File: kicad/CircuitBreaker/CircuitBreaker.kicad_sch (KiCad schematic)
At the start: 57 parts, among them J1 PH2.54, J10 Conn_01x04_uplink, J4 PH2.54, J5 Conn_01x04_downlink, J6 Conn_01x04_downlink, J7 PH2.54, J9 Conn_01x04_uplink, SW1 usbIAP, T1 CT104D, T2 CT104D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

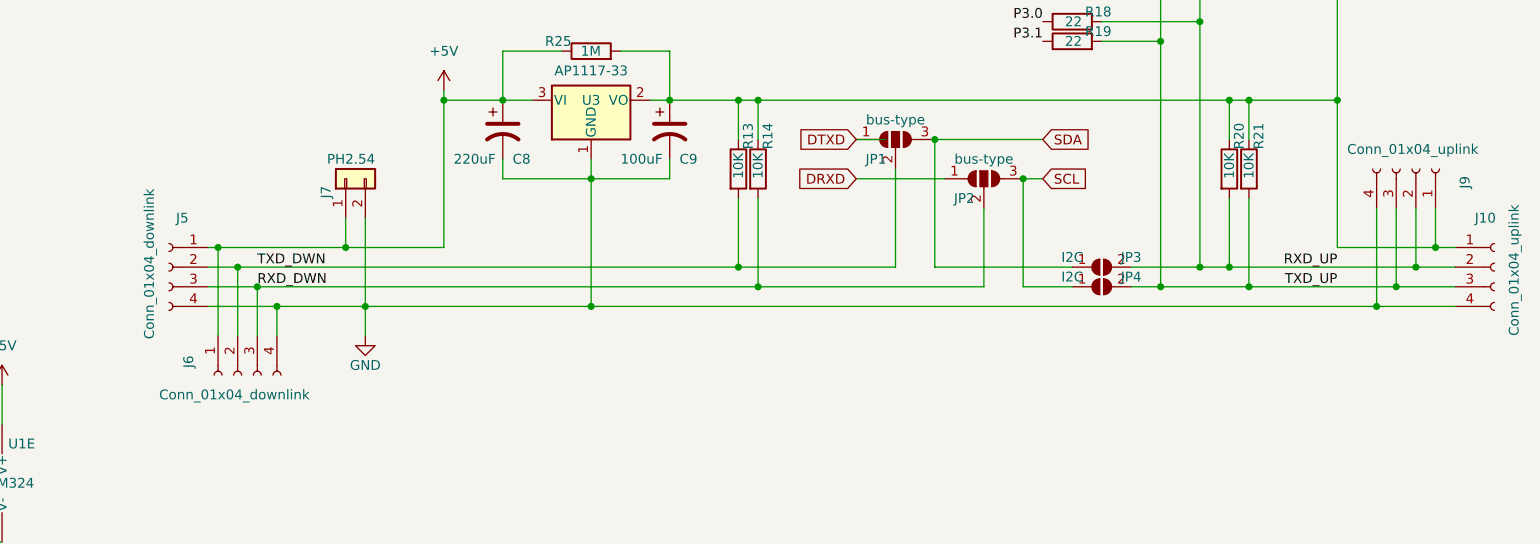
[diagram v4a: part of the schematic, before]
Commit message: net mapped to pcb
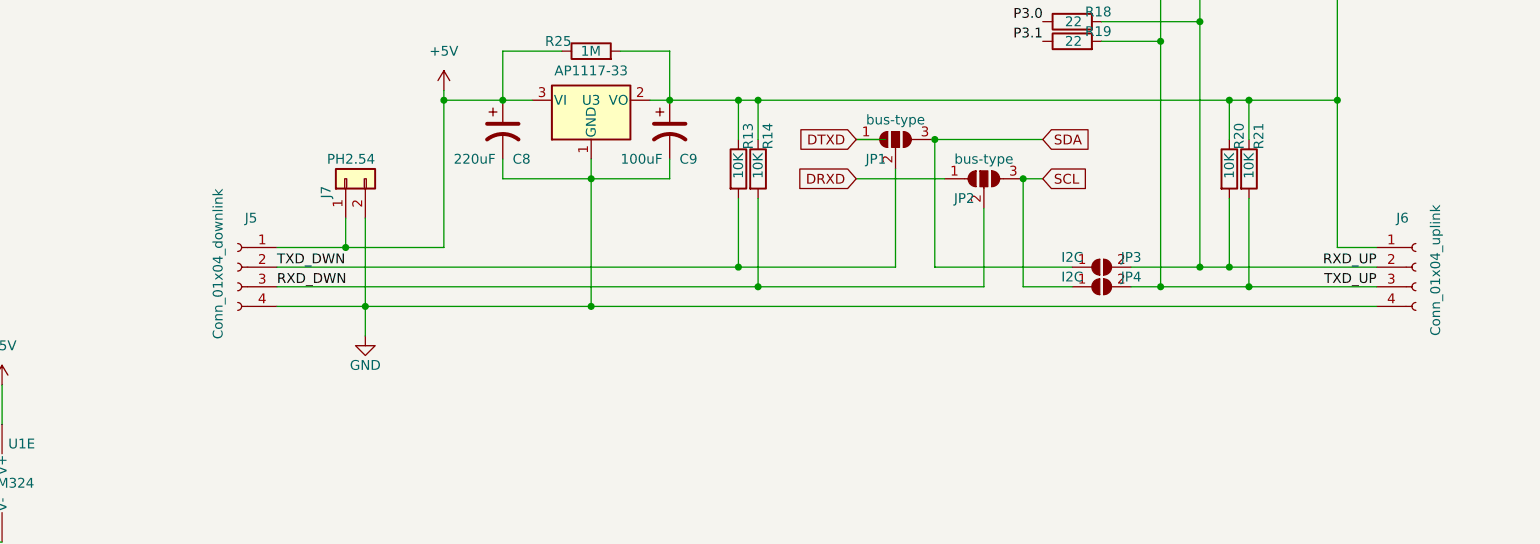
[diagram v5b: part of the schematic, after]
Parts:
- removed J6: Conn_01x04_downlink, Connector_PinHeader_2.00mm:PinHeader_1x04_P2.00mm_Vertical, symbol Connector:Conn_01x04_Female
- removed J9: Conn_01x04_uplink, Connector_PinSocket_2.00mm:PinSocket_1x04_P2.00mm_Vertical, symbol Connector:Conn_01x04_Female
- C1, C10, C2, C3, C4, C5, C6: footprint Capacitor_SMD:C_0201_0603Metric -> Capacitor_SMD:C_0603_1608Metric
- J7: footprint Connector_PinSocket_2.54mm:PinSocket_1x02_P2.54mm_Vertical_SMD_Pin1Left -> Connector_PinHeader_2.54mm:PinHeader_1x02_P2.54mm_Vertical
- R10, R11, R12, R13, R14, R15, R17, R18, R19, R20, R21, R22, R23, R24, R9: footprint Resistor_SMD:R_0201_0603Metric -> Resistor_SMD:R_0603_1608Metric
- R16: footprint Resistor_SMD:R_0201_0603Metric -> Resistor_SMD:R_0805_2012Metric
- renumbered J10 to J6
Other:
- moved on the sheet: J5, J6

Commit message: pcb rev
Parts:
- added D1: green, LED_SMD:LED_0603_1608Metric, symbol Device:LED
- added D2: blue, LED_SMD:LED_0603_1608Metric, symbol Device:LED
- added R26, R27: 4K7, Resistor_SMD:R_0603_1608Metric, symbol Device:R
- JP5, JP6: footprint Jumper:SolderJumper-2_P1.3mm_Open_RoundedPad1.0x1.5mm -> Jumper:SolderJumper-2_P1.3mm_Bridged_RoundedPad1.0x1.5mm
- R1, R2, R3, R7: footprint Resistor_THT:R_Axial_DIN0204_L3.6mm_D1.6mm_P1.90mm_Vertical -> Resistor_THT:R_Axial_DIN0204_L3.6mm_D1.6mm_P7.62mm_Horizontal
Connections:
- net +5V: now also D1.2 (A), D2.2 (A)
- net at U2.17 (P3.6/ADC14/RxD_2): now also R27.1
- net at U2.18 (P3.7/INT3/TxD_2): now also R26.1
- new net: D2.1 (K), R27.2
- new net: D1.1 (K), R26.2
- no-connect marks 27 -> 25
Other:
- moved on the sheet: C1, C10, C2, C3, C4, C5, C6, C7, C8, C9, J1, J4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

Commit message: pcb all connected
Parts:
- R25: value 1M -> 5vUP
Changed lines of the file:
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@@
       (effects (font (size 1.27 1.27)) (justify left))
     )
-    (property "Value" "1M" (id 1) (at 151.13 119.38 90)
+    (property "Value" "5vUP" (id 1) (at 151.13 119.38 90)
       (effects (font (size 1.27 1.27)) (justify left))
     )
@@
     )
     (path "/b9254481-42de-41b8-8b47-4a505cebb15c"
-      (reference "R25") (unit 1) (value "1M") (footprint "Resistor_SMD:R_0805_2012Metric")
+      (reference "R25") (unit 1) (value "5vUP") (footprint "Resistor_SMD:R_0805_2012Metric")
     )
     (path "/e07fefd4-5202-4e30-b6e7-2e0271b2c212"

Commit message: silklayers review
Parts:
- D1: value green -> grn
- D2: value blue -> blu
- J5: value Conn_01x04_downlink -> downlink
- J6: value Conn_01x04_uplink -> uplink
- J7: value PH2.54 -> PWN-In-5v
- U2: value STC8H8K64U-45I-TSSOP20 -> STC8H8K64U
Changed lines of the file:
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@@
       (effects (font (size 1.27 1.27)) (justify right))
     )
-    (property "Value" "blue" (id 1) (at 187.96 44.45 0)
+    (property "Value" "blu" (id 1) (at 187.96 44.45 0)
       (effects (font (size 1.27 1.27)) (justify right))
     )
@@
       (effects (font (size 1.27 1.27)) (justify left))
     )
-    (property "Value" "PH2.54" (id 1) (at 125.73 133.35 90)
+    (property "Value" "PWN-In-5v" (id 1) (at 125.73 133.35 90)
       (effects (font (size 1.27 1.27)) (justify left))
     )
@@
     (in_bom yes) (on_board yes)
     (property "Reference" "U2" (id 0) (at 146.05 43.18 0))
-    (property "Value" "STC8H8K64U-45I-TSSOP20" (id 1) (at 146.05 78.74 0))
+    (property "Value" "STC8H8K64U" (id 1) (at 146.05 78.74 0))
     (property "Footprint" "Package_SO:TSSOP-20_4.4x5mm_P0.4mm" (id 2) (at 139.7 64.77 0)
       (effects (font (size 1.27 1.27)) hide)
@@
       (effects (font (size 1.27 1.27)) (justify right))
     )
-    (property "Value" "green" (id 1) (at 184.15 44.45 0)
+    (property "Value" "grn" (id 1) (at 184.15 44.45 0)
       (effects (font (size 1.27 1.27)) (justify right))
     )
@@
       (effects (font (size 1.27 1.27)) (justify left))
     )
-    (property "Value" "Conn_01x04_uplink" (id 1) (at 276.86 156.21 90)
+    (property "Value" "uplink" (id 1) (at 275.59 146.05 90)
       (effects (font (size 1.27 1.27)) (justify left))
     )
@@
       (effects (font (size 1.27 1.27)) (justify left))
     )
-    (property "Value" "Conn_01x04_downlink" (id 1) (at 105.41 137.16 90)
+    (property "Value" "downlink" (id 1) (at 105.41 137.16 90)
       (effects (font (size 1.27 1.27)) (justify right))
     )
@@
     )
     (path "/5043d550-329f-4c22-af2e-a891b18ddb8a"
-      (reference "D1") (unit 1) (value "green") (footprint "LED_SMD:LED_0603_1608Metric")
+      (reference "D1") (unit 1) (value "grn") (footprint "LED_SMD:LED_0603_1608Metric")
     )
     (path "/222a9ad1-ac03-480c-938b-316b28742e5a"
-      (reference "D2") (unit 1) (value "blue") (footprint "LED_SMD:LED_0603_1608Metric")
+      (reference "D2") (unit 1) (value "blu") (footprint "LED_SMD:LED_0603_1608Metric")
     )
     (path "/ed5e7f7b-7ab0-466d-9f53-71c8cd09f405"
@@
     )
     (path "/c07a5c95-f059-4fa8-ba50-b8c87ea51725"
-      (reference "J5") (unit 1) (value "Conn_01x04_downlink") (footprint "Connector_PinHeader_2.00mm:PinHeader_1x04_P2.00mm_Vertical")
+      (reference "J5") (unit 1) (value "downlink") (footprint "Connector_PinHeader_2.00mm:PinHeader_1x04_P2.00mm_Vertical")
     )
     (path "/8d7c933c-f4ee-46e2-8572-6e1196f4bf56"
-      (reference "J6") (unit 1) (value "Conn_01x04_uplink") (footprint "Connector_PinSocket_2.00mm:PinSocket_1x04_P2.00mm_Vertical")
+      (reference "J6") (unit 1) (value "uplink") (footprint "Connector_PinSocket_2.00mm:PinSocket_1x04_P2.00mm_Vertical")
     )
     (path "/3c5fb37c-c9c3-4123-899a-868e80eda11f"
-      (reference "J7") (unit 1) (value "PH2.54") (footprint "Connector_PinHeader_2.54mm:PinHeader_1x02_P2.54mm_Vertical")
+      (reference "J7") (unit 1) (value "PWN-In-5v") (footprint "Connector_PinHeader_2.54mm:PinHeader_1x02_P2.54mm_Vertical")
     )
     (path "/f6fabe2b-8561-4cc8-8c90-c9ae9db53609"
@@
     )
     (path "/4a27f6f5-b0e4-4aa4-a25b-c8f6fbf1beb6"
-      (reference "U2") (unit 1) (value "STC8H8K64U-45I-TSSOP20") (footprint "Package_SO:TSSOP-20_4.4x5mm_P0.4mm")
+      (reference "U2") (unit 1) (value "STC8H8K64U") (footprint "Package_SO:TSSOP-20_4.4x5mm_P0.4mm")
     )
     (path "/06ee62ce-0f50-4fac-8235-fc1e35a64b1b"
